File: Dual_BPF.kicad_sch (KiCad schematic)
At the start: 131 parts, among them J1 Conn_Coaxial, J2 Conn_Coaxial, J3 Conn_02x05_Odd_Even, K1 EE2-12NU, K10 EE2-12NU, K11 EE2-12NU, K12 EE2-12NU, K13 EE2-12NU, K14 EE2-12NU, K15 EE2-12NU, K2 EE2-12NU, K3 EE2-12NU, K4 EE2-12NU, K5 EE2-12NU, K6 EE2-12NU, K7 EE2-12NU, K8 EE2-12NU, K9 EE2-12NU, Q1 BSP250 /ZVP2106, U1 PGA-103, U2 RLP-30

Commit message: work in progress, 2 different pcb
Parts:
- removed D2: CD05_SOD323-T05, Diode_SMD:D_SOD-323, symbol Diode:SD05_SOD323
- removed K1, K10, K11, K12, K13, K14, K15, K2, K3, K4, K5, K6, K7, K8, K9: EE2-12NU, Relay_SMD:Relay_DPDT_Kemet_EE2_NU, symbol Relay:EE2-12NU
- removed U2: RLP-30, RF_Mini-Circuits:Mini-Circuits_GP1212_LandPatternPL-176, symbol RF_Filter:RLP-30
- added C100, C101, C102, C103, C104, C105, C106, C107, C108, C55, C56, C57, C58, C59, C60, C61, C62, C63, C64, C65, C66, C67, C68, C93, C94, C95, C96, C97, C98, C99: 10n, Capacitor_SMD:C_0805_2012Metric_Pad1.18x1.45mm_HandSolder, symbol Device:C_Small
- added C69, C71, C79: 100p, Capacitor_SMD:C_0805_2012Metric_Pad1.18x1.45mm_HandSolder, symbol Device:C_Small
- added C70, C73, C81, C92: 100n, Capacitor_SMD:C_0805_2012Metric_Pad1.18x1.45mm_HandSolder, symbol Device:C_Small
- added C72, C75, C88, C91: 470p, Capacitor_SMD:C_0805_2012Metric_Pad1.18x1.45mm_HandSolder, symbol Device:C_Small
- added C74, C87: 1n, Capacitor_SMD:C_0805_2012Metric_Pad1.18x1.45mm_HandSolder, symbol Device:C_Small
- added C76, C89: 270p, Capacitor_SMD:C_0805_2012Metric_Pad1.18x1.45mm_HandSolder, symbol Device:C_Small
- added C77, C78, C86, C90: 220p, Capacitor_SMD:C_0805_2012Metric_Pad1.18x1.45mm_HandSolder, symbol Device:C_Small
- added C80: 390p, Capacitor_SMD:C_0805_2012Metric_Pad1.18x1.45mm_HandSolder, symbol Device:C_Small
- added C82: 680p, Capacitor_SMD:C_0805_2012Metric_Pad1.18x1.45mm_HandSolder, symbol Device:C_Small
- added C83: 180p, Capacitor_SMD:C_0805_2012Metric_Pad1.18x1.45mm_HandSolder, symbol Device:C_Small
- added C84: 82p, Capacitor_SMD:C_0805_2012Metric_Pad1.18x1.45mm_HandSolder, symbol Device:C_Small
- added C85: 47p, Capacitor_SMD:C_0805_2012Metric_Pad1.18x1.45mm_HandSolder, symbol Device:C_Small
- added D2: SS36, Diode_SMD:D_SMB, symbol Device:D_Small
- added FB31, FB32, FB33, FB34, FB35, FB36, FB37, FB38, FB39, FB40, FB41, FB42, FB43, FB44, FB45, FB46, FB47, FB48, FB49, FB50, FB51, FB52, FB53, FB54, FB55, FB56, FB57, FB58, FB59, FB60: Ferrite, Inductor_SMD:L_0805_2012Metric, symbol Device:FerriteBead_Small
- added H1, H2, H3, H4, H5, H6, H7, H8: MountingHole_Pad, MountingHole:MountingHole_3.2mm_M3_ISO14580_Pad, symbol Mechanical:MountingHole_Pad
- added J4, J5: Conn_Coaxial, SMA_PINS:SMA_PINS, symbol Connector:Conn_Coaxial
- added J6: Conn_02x05_Odd_Even, Connector_IDC:IDC-Header_2x05_P2.54mm_Vertical, symbol Connector_Generic:Conn_02x05_Odd_Even
- added K1, K10, K11, K12, K13, K14, K15, K16, K17, K18, K19, K2, K20, K21, K22, K23, K24, K25, K26, K27, K28, K29, K3, K30, K4, K5, K6, K7, K8, K9: EC2-12NU, Relay_THT:Relay_DPDT_Kemet_EC2, symbol Relay:EC2-12NU
- added L18, L22, L24, L32: 330n, Inductor_SMD:L_1812_4532Metric_Pad1.30x3.40mm_HandSolder, symbol Device:L_Small
- added L19, L29, L34: 10u, Inductor_SMD:L_1812_4532Metric_Pad1.30x3.40mm_HandSolder, symbol Device:L_Small
- added L20, L26, L30: 1.8u, Inductor_SMD:L_1812_4532Metric_Pad1.30x3.40mm_HandSolder, symbol Device:L_Small
- added L21, L28, L31: 680n, Inductor_SMD:L_1812_4532Metric_Pad1.30x3.40mm_HandSolder, symbol Device:L_Small
- added L23, L33: 150n, Inductor_SMD:L_1812_4532Metric_Pad1.30x3.40mm_HandSolder, symbol Device:L_Small
- added L25: 2.7u, Inductor_SMD:L_1812_4532Metric_Pad1.30x3.40mm_HandSolder, symbol Device:L_Small
- added L27: 1u, Inductor_SMD:L_1812_4532Metric_Pad1.30x3.40mm_HandSolder, symbol Device:L_Small
- added Q2: BSP250 /ZVP2106, Package_TO_SOT_SMD:SOT-223-3_TabPin2, symbol Transistor_FET:FQP27P06
- added R10: 10k, Resistor_SMD:R_0805_2012Metric_Pad1.20x1.40mm_HandSolder, symbol Device:R_Small
- added R11, R12, R14, R18, R2, R3: 100R, Resistor_SMD:R_0805_2012Metric_Pad1.20x1.40mm_HandSolder, symbol Device:R_Small
- added R13, R15, R16: 62R, Resistor_SMD:R_0805_2012Metric_Pad1.20x1.40mm_HandSolder, symbol Device:R_Small
- added R17: 30R, Resistor_SMD:R_0805_2012Metric_Pad1.20x1.40mm_HandSolder, symbol Device:R_Small
- added U2: PGA-103, Package_TO_SOT_SMD:SOT-89-3, symbol RF_Amplifier:PGA-103
- C15, C17: value C_Small -> 100p
- C16, C19: value C_Small -> 100n
- C18, C21: value C_Small -> 470p
- C20: value C_Small -> 1n
- C22: value C_Small -> 270p
- C23, C24: value C_Small -> 220p
- C25: renamed from C26; value C_Small -> 100p
- C26: renamed from C27; value C_Small -> 390p
- C27: renamed from C28; value C_Small -> 100n
- C28: renamed from C29; value C_Small -> 680p
- C29: renamed from C30; value C_Small -> 180p
- C30: renamed from C31; value C_Small -> 82p
- C31: renamed from C32; value C_Small -> 47p
- C32: renamed from C33; value C_Small -> 220p
- C33: renamed from C35; value C_Small -> 1n
- C34: renamed from C36; value C_Small -> 470p
- C35: renamed from C37; value C_Small -> 270p
- C36: renamed from C38; value C_Small -> 220p
- C37: renamed from C39; value C_Small -> 470p
- C38: renamed from C25; value C_Small -> 100n
- D1: value D_Small -> SS36; footprint (none) -> Diode_SMD:D_SMB
- FB1, FB10, FB11, FB12, FB13, FB14, FB15, FB16, FB17, FB18, FB19, FB2, FB20, FB21, FB22, FB23, FB24, FB25, FB26, FB27, FB28, FB29, FB3, FB30, FB4, FB5, FB6, FB7, FB8, FB9: footprint (none) -> Inductor_SMD:L_0805_2012Metric
- J1, J2: footprint (none) -> SMA_PINS:SMA_PINS
- J3: footprint (none) -> Connector_IDC:IDC-Header_2x05_P2.54mm_Vertical
- L1, L15, L5, L7: value L_Small -> 330n; footprint (none) -> Amidon_T50:T50_V_THT_1812_merge
- L10: value L_Small -> 1u; footprint (none) -> Amidon_T50:T50_V_THT_1812_merge
- L11, L14, L4: value L_Small -> 680n; footprint (none) -> Amidon_T50:T50_V_THT_1812_merge
- L12, L17, L2: value L_Small -> 10u; footprint (none) -> Amidon_T50:T50_V_THT_1812_merge
- L13, L3, L9: value L_Small -> 1.8u; footprint (none) -> Amidon_T50:T50_V_THT_1812_merge
- L16, L6: value L_Small -> 150n; footprint (none) -> Amidon_T50:T50_V_THT_1812_merge
- L8: value L_Small -> 2.7u; footprint (none) -> Amidon_T50:T50_V_THT_1812_merge
- Q1: footprint Package_TO_SOT_THT:TO-220-3_Vertical -> Package_TO_SOT_SMD:SOT-223-3_TabPin2
- R1: renamed from R4; value R_Small -> 10k; footprint (none) -> Resistor_SMD:R_0805_2012Metric_Pad1.20x1.40mm_HandSolder
- R4: renamed from R2; value R_Small -> 62R; footprint (none) -> Resistor_SMD:R_0805_2012Metric_Pad1.20x1.40mm_HandSolder
- R5: renamed from R1; value R_Small -> 100R; footprint (none) -> Resistor_SMD:R_0805_2012Metric_Pad1.20x1.40mm_HandSolder
- R6: renamed from R3; value R_Small -> 62R; footprint (none) -> Resistor_SMD:R_0805_2012Metric_Pad1.20x1.40mm_HandSolder
- R7: renamed from R5; value R_Small -> 62R; footprint (none) -> Resistor_SMD:R_0805_2012Metric_Pad1.20x1.40mm_HandSolder
- R8: renamed from R6; value R_Small -> 30R; footprint (none) -> Resistor_SMD:R_0805_2012Metric_Pad1.20x1.40mm_HandSolder
- R9: renamed from R7; value R_Small -> 100R; footprint (none) -> Resistor_SMD:R_0805_2012Metric_Pad1.20x1.40mm_HandSolder
- renumbered C40 to C39, C41 to C40, C42 to C41, C43 to C42, C44 to C43, C45 to C44, C46 to C45, C47 to C46, C48 to C47, C49 to C48, C50 to C49, C51 to C50, C52 to C51, C34 to C52
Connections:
- net +12V: now also C81.1, FB32.1, FB34.1, FB36.1, FB38.1, FB40.1, FB42.1, FB44.1, FB46.1, FB48.1, FB50.1, FB52.1, FB54.1, FB56.1, FB58.1, FB60.1, J6.9 (Pin_9), Q2.3 (S), R10.1
- net 1.5HPF: now also FB33.1, FB47.1, J6.5 (Pin_5)
- net 13HPF: now also FB39.1, FB53.1, J6.2 (Pin_2)
- net 20HPF: now also FB41.1, FB55.1, J6.1 (Pin_1)
- net 6.5HPF: now also FB35.1, FB49.1, J6.4 (Pin_4)
- net 6mLNA: now also C70.1, D2.1 (K), FB31.1, FB59.1, J6.6 (Pin_6)
- net 9.5HPF: now also FB37.1, FB51.1, J6.3 (Pin_3)
- net GND: now also C100.2, C101.2, C102.2, C103.2, C104.2, C105.2, C106.1, C107.2, C108.2, C55.2, C56.2, C57.2, C58.2, C59.2, C60.2, C61.2, C62.2, C63.2, C64.2, C65.2, C66.2, C67.2, C68.2, C70.2, C72.2, C73.1, C74.2, C75.2, C76.2, C77.2, C80.1, C81.2, C87.1, C88.1, C89.1, C90.1, C91.2, C93.2, C94.2, C95.2, C96.2, C97.2, C98.2, C99.2, H1.1, H2.1, H3.1, H4.1, H5.1, H6.1, H7.1, H8.1, J4.2 (Ext), J5.2 (Ext), J6.10 (Pin_10), K1.10, K1.3, K10.10, K10.3, K11.10, K11.3, K12.10, K12.3, K13.10, K13.3, K14.10, K14.3, K15.10, K15.3, K16.10, K16.3, K17.10, K17.3, K18.10, K18.3, K19.10, K19.3, K2.10, K2.3, K20.10, K20.3, K21.10, K21.3, K22.10, K22.3, K24.10, K24.3, K25.10, K25.3, K26.10, K26.3, K27.10, K27.3, K28.10, K28.3, K29.10, K29.3, K3.10, K3.3, K30.10, K30.3, K4.10, K4.3, K5.10, K5.3, K6.10, K6.3, K7.10, K7.3, K9.10, K9.3, L18.2, L20.1, L21.1, L22.1, L23.1, L24.2, L29.2, L30.2, L31.2, L32.2, L33.2, R11.2, R12.1, R14.2, R18.1, R2.2, R3.1, U2.2 (GND)
- net HPF_ByPass: now also FB43.1, FB57.1, J6.8 (Pin_8)
- net RX2_GND: now also FB45.1, J6.7 (Pin_7)
- net at C12.1, FB10.2: now also K5.1
- net at C6.1, FB9.2: now also K5.12
- net at C22.1, L10.1, L5.2: now also K5.4, K5.9
- net at C29.1, C34.2, L14.1: now also K11.4, K11.9
- net at C49.1, FB23.2: now also K12.12
- net at C52.2, FB16.2: now also K8.1
- net at C39.1, FB15.2: now also K8.12
- net at J2.1 (In): now also K8.10, K8.3, K8.5, K8.8, R2.1, R3.2
- net at C25.1, U1.1: no longer C38.1, R7.2
- net at U1.3: now also C38.2, R7.2; no longer R8.2
- net at C43.1, FB24.2: now also K12.1
- net at C41.1, FB20.2: now also K10.1
- net at C30.1, C35.2, L15.1: now also K12.4, K12.9
- net at C53.1, FB30.2: now also K15.1
- net at C44.1, FB26.2: now also K13.1
- net at C46.1, FB17.2: now also K9.12
- net at C28.1, C33.2, L13.1: now also K10.4, K10.9
- net at C21.1, L4.2, L9.1: now also K4.4, K4.9
- net at C15.2: now also K1.4, K1.9
- net at C54.1, FB29.2: now also K15.12
- net at J1.1 (In): now also K10.5, K10.8, K11.5, K11.8, K12.5, K12.8, K13.5, K13.8, K14.5, K14.8, K15.5, K15.8, K9.5, K9.8
- net at C9.1, FB4.2: now also K2.1
- net at C47.1, FB19.2: now also K10.12
- net at C31.1, C36.2, L16.1: now also K13.4, K13.9
- net at C45.1, FB28.2: now also K14.1
- net at R5.1: now also C38.1, R8.2; no longer C38.2
- net at C1.1, FB1.2: now also K1.12
- net at R8.1, R9.2: now also K15.4, K15.9
- net at C13.1, FB12.2: now also K6.1
- net at C8.1, FB13.2: now also K7.12
- net at C10.1, FB6.2: now also K3.1
- net at L2.2: now also K2.4, K2.9
- net at C2.1, FB2.2: now also K1.1
- net at L17.1: now also K9.4, K9.9
- net at C20.1, L3.2, L8.1: now also K3.4, K3.9
- net at C50.1, FB25.2: now also K13.12
- net at C7.1, FB11.2: now also K6.12
- net at C11.1, FB8.2: now also K4.1
- net at C4.1, FB5.2: now also K3.12
- net at C42.1, FB22.2: now also K11.1
- net at C14.1, FB14.2: now also K7.1
- net at C40.1, FB18.2: now also K9.1
- net at C51.1, FB27.2: now also K14.12
- net at C23.1, L11.1, L6.2: now also K6.4, K6.9
- net at C5.1, FB7.2: now also K4.12
- net at C48.1, FB21.2: now also K11.12
- net at C3.1, FB3.2: now also K2.12
- new net: C68.1, FB44.2, K22.1
- new net: J5.1 (In), K23.10, K23.3
- new net: C108.1, FB59.2, K30.12
- new net: C65.1, FB38.2, K19.1
- new net: C59.1, FB37.2, K19.12
- new net: C75.1, K19.4, K19.9, L21.2, L26.1
- new net: K16.5, K16.8, K17.5, K17.8, K18.5, K18.8, K19.5, K19.8, K20.5, K20.8, K21.5, K21.8, K22.5, K22.8, K23.4, K23.9
- new net: K1.5, K1.8, K2.5, K2.8, K3.5, K3.8, K4.5, K4.8, K5.5, K5.8, K6.5, K6.8, K7.5, K7.8, K8.4, K8.9
- new net: C74.1, K18.4, K18.9, L20.2, L25.1
- new net: C82.2, L25.2
- new net: C84.1, C89.2, K27.4, K27.9, L32.1
- new net: C57.1, FB33.2, K17.12
- new net: C58.1, FB35.2, K18.12
- new net: C86.2, C91.1, L34.2
- new net: C77.1, K21.4, K21.9, L23.2, L28.1
- new net: C69.1, C71.2, L18.1
- new net: C101.1, FB49.2, K25.12
- new net: C85.2, L28.2
- new net: C83.2, L26.2
- new net: K14.4, K14.9, K7.4, K7.9
- new net: K23.5, K23.8, R11.1, R12.2
- new net: C85.1, C90.2, K28.4, K28.9, L33.1
- new net: C61.1, FB41.2, K21.12
- new net: C63.1, FB34.2, K17.1
- new net: K17.4, K17.9, L19.2
- new net: C92.1, R14.1, R17.2
- new net: C83.1, C88.2, K26.4, K26.9, L31.1
- new net: C67.1, FB42.2, K21.1
- new net: C55.1, FB31.2, K16.12
- new net: K24.4, K24.9, L34.1
- new net: C66.1, FB40.2, K20.1
- new net: C60.1, FB39.2, K20.12
- new net: C76.1, K20.4, K20.9, L22.2, L27.1
- new net: C69.2, K16.4, K16.9
- new net: C95.1, FB50.2, K25.1
- new net: C82.1, C87.2, K25.4, K25.9, L30.1
- new net: J4.1 (In), K24.5, K24.8, K25.5, K25.8, K26.5, K26.8, K27.5, K27.8, K28.5, K28.8, K29.5, K29.8, K30.5, K30.8
- new net: C78.2, C80.2, C86.1, L29.1
- new net: R15.2, R16.1
- new net: C92.2, R16.2, U2.3
- new net: C72.1, C78.1, L19.1
- new net: C84.2, L27.2
- new net: C93.1, FB45.2, K23.12
- new net: C103.1, FB53.2, K27.12
- new net: K30.4, K30.9, R17.1, R18.2
- new net: C71.1, C79.2, L24.1
- new net: C96.1, FB52.2, K26.1
- new net: C102.1, FB51.2, K26.12
- new net: C97.1, FB54.2, K27.1
- new net: C106.2, FB46.2, K23.1
- new net: C64.1, FB36.2, K18.1
- new net: C107.1, FB60.2, K30.1
- new net: C62.1, FB43.2, K22.12
- new net: C73.2, Q2.2 (D), R13.1
- new net: R13.2, R15.1
- new net: D2.2 (A), Q2.1 (G), R10.2
- new net: C94.1, FB48.2, K24.1
- new net: C105.1, FB57.2, K29.12
- new net: C104.1, FB55.2, K28.12
- new net: C79.1, U2.1
- new net: C98.1, FB56.2, K28.1
- new net: C100.1, FB47.2, K24.12
- new net: C99.1, FB58.2, K29.1
- new net: K22.4, K22.9, K29.4, K29.9
- new net: C56.1, FB32.2, K16.1
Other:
- note added: "All relays EE2-12NU (gull wing) or EC2-12NU (through)"
- note removed: "SOD-323-2"
- moved on the sheet: C38, C39, C52, FB15, FB16, J2, R4, R5, R6, R7, R8, R9

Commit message: SMD version RTM 1.0, toroid version deleted
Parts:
- removed C1, C10, C11, C12, C13, C14, C2, C3, C39, C4, C40, C41, C42, C43, C44, C45, C46, C47, C48, C49, C5, C50, C51, C52, C53, C54, C6, C7, C8, C9: 10n, Capacitor_SMD:C_0805_2012Metric_Pad1.18x1.45mm_HandSolder, symbol Device:C_Small
- removed C15, C17, C25: 100p, Capacitor_SMD:C_0805_2012Metric_Pad1.18x1.45mm_HandSolder, symbol Device:C_Small
- removed C16, C19, C27, C38: 100n, Capacitor_SMD:C_0805_2012Metric_Pad1.18x1.45mm_HandSolder, symbol Device:C_Small
- removed C18, C21, C34, C37: 470p, Capacitor_SMD:C_0805_2012Metric_Pad1.18x1.45mm_HandSolder, symbol Device:C_Small
- removed C20, C33: 1n, Capacitor_SMD:C_0805_2012Metric_Pad1.18x1.45mm_HandSolder, symbol Device:C_Small
- removed C22, C35: 270p, Capacitor_SMD:C_0805_2012Metric_Pad1.18x1.45mm_HandSolder, symbol Device:C_Small
- removed C23, C24, C32, C36: 220p, Capacitor_SMD:C_0805_2012Metric_Pad1.18x1.45mm_HandSolder, symbol Device:C_Small
- removed C26: 390p, Capacitor_SMD:C_0805_2012Metric_Pad1.18x1.45mm_HandSolder, symbol Device:C_Small
- removed C28: 680p, Capacitor_SMD:C_0805_2012Metric_Pad1.18x1.45mm_HandSolder, symbol Device:C_Small
- removed C29: 180p, Capacitor_SMD:C_0805_2012Metric_Pad1.18x1.45mm_HandSolder, symbol Device:C_Small
- removed C30: 82p, Capacitor_SMD:C_0805_2012Metric_Pad1.18x1.45mm_HandSolder, symbol Device:C_Small
- removed C31: 47p, Capacitor_SMD:C_0805_2012Metric_Pad1.18x1.45mm_HandSolder, symbol Device:C_Small
- removed D1: SS36, Diode_SMD:D_SMB, symbol Device:D_Small
- removed FB1, FB10, FB11, FB12, FB13, FB14, FB15, FB16, FB17, FB18, FB19, FB2, FB20, FB21, FB22, FB23, FB24, FB25, FB26, FB27, FB28, FB29, FB3, FB30, FB4, FB5, FB6, FB7, FB8, FB9: Ferrite, Inductor_SMD:L_0805_2012Metric, symbol Device:FerriteBead_Small
- removed H1, H2, H3, H4: MountingHole_Pad, MountingHole:MountingHole_3.2mm_M3_ISO14580_Pad, symbol Mechanical:MountingHole_Pad
- removed J1, J2: Conn_Coaxial, SMA_PINS:SMA_PINS, symbol Connector:Conn_Coaxial
- removed J3: Conn_02x05_Odd_Even, Connector_IDC:IDC-Header_2x05_P2.54mm_Vertical, symbol Connector_Generic:Conn_02x05_Odd_Even
- removed K1, K10, K11, K12, K13, K14, K15, K2, K3, K4, K5, K6, K7, K8, K9: EC2-12NU, Relay_THT:Relay_DPDT_Kemet_EC2, symbol Relay:EC2-12NU
- removed L1, L15, L5, L7: 330n, Amidon_T50:T50_V_THT_1812_merge, symbol Device:L_Small
- removed L10: 1u, Amidon_T50:T50_V_THT_1812_merge, symbol Device:L_Small
- removed L11, L14, L4: 680n, Amidon_T50:T50_V_THT_1812_merge, symbol Device:L_Small
- removed L12, L17, L2: 10u, Amidon_T50:T50_V_THT_1812_merge, symbol Device:L_Small
- removed L13, L3, L9: 1.8u, Amidon_T50:T50_V_THT_1812_merge, symbol Device:L_Small
- removed L16, L6: 150n, Amidon_T50:T50_V_THT_1812_merge, symbol Device:L_Small
- removed L8: 2.7u, Amidon_T50:T50_V_THT_1812_merge, symbol Device:L_Small
- removed Q1: BSP250 /ZVP2106, Package_TO_SOT_SMD:SOT-223-3_TabPin2, symbol Transistor_FET:FQP27P06
- removed R1: 10k, Resistor_SMD:R_0805_2012Metric_Pad1.20x1.40mm_HandSolder, symbol Device:R_Small
- removed R2, R3, R5, R9: 100R, Resistor_SMD:R_0805_2012Metric_Pad1.20x1.40mm_HandSolder, symbol Device:R_Small
- removed R4, R6, R7: 62R, Resistor_SMD:R_0805_2012Metric_Pad1.20x1.40mm_HandSolder, symbol Device:R_Small
- removed R8: 30R, Resistor_SMD:R_0805_2012Metric_Pad1.20x1.40mm_HandSolder, symbol Device:R_Small
- removed U1: PGA-103, Package_TO_SOT_SMD:SOT-89-3, symbol RF_Amplifier:PGA-103
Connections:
- net 1.5HPF renamed 1.5HPF_2
- net 13HPF renamed 13HPF_2
- net 20HPF renamed 20HPF_2
- net 6.5HPF renamed 6.5HPF_2
- net 6mLNA renamed 6mLNA_2
- net 9.5HPF renamed 9.5HPF_2
- net HPF_ByPass renamed HPF_ByPass_2
- net RX2_GND renamed RX2_GND_2
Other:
- moved on the sheet: C100, C101, C102, C103, C104, C105, C106, C107, C108, C55, C56, C57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

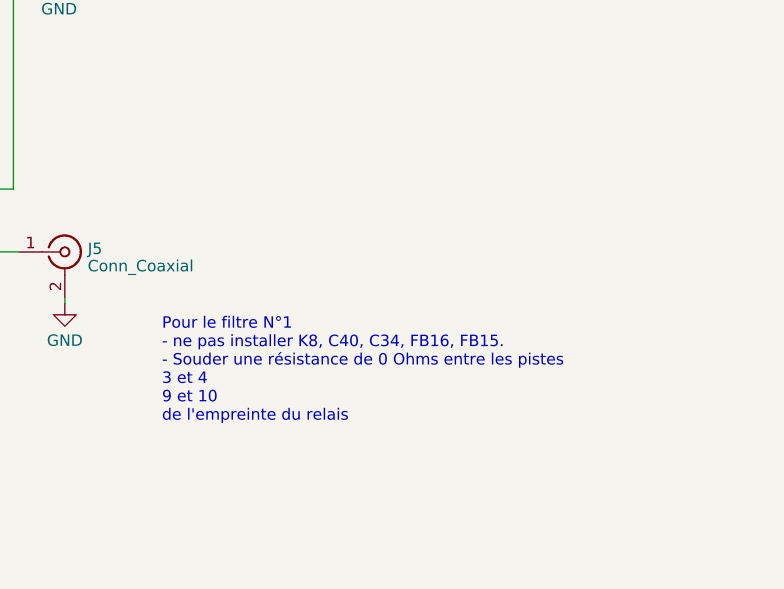
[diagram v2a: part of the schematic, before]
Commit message: small mods on schematic comments
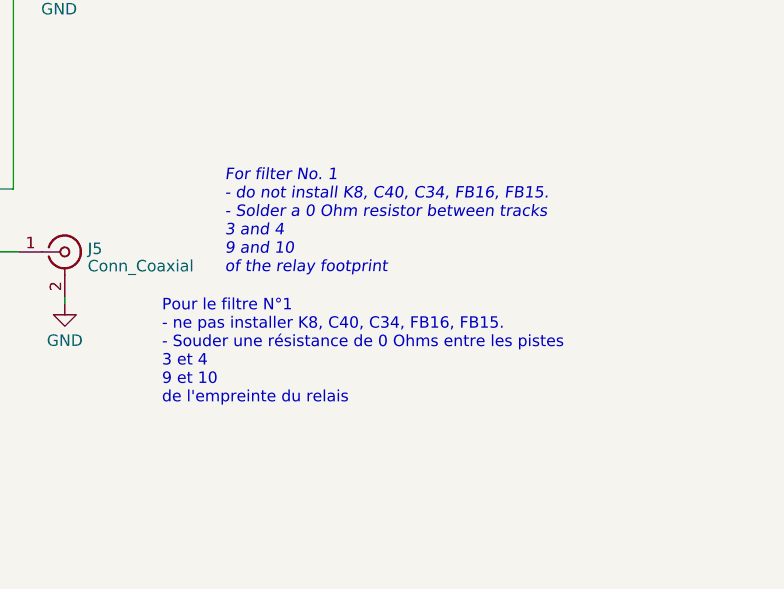
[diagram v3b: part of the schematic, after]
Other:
- note added: "For filter No. 1 - do not install K8, C40, C34, FB16, FB15. - Solder a 0 Ohm resistor between tracks 3 and 4 9 and 10 of the relay footprint"
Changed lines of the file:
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@@
     (stroke (width 0) (type default))
   )
-  (text "Pour le filtre N°1\n- ne pas installer K8, C40, C34, FB16, FB15. \n- Souder une résistance de 0 Ohms entre les pistes \n3 et 4\n9 et 10 \nde l'empreinte du relais"
+  (text "Pour le filtre N°1\n- ne pas installer K8, C40, C34, FB16, FB15. \n- Souder une résistance de 0 Ohms entre les pistes \n3 et 4\n9 et 10 \nde l'empreinte du relais\n\n"
     (at 145.415 247.65 0)
     (effects (font (size 1.27 1.27)) (justify left bottom))
@@
     (effects (font (size 1.27 1.27)) (justify left bottom))
   )
+  (text "For filter No. 1\n- do not install K8, C40, C34, FB16, FB15. \n- Solder a 0 Ohm resistor between tracks \n3 and 4\n9 and 10 \nof the relay footprint"
+    (at 152.4 231.14 0)
+    (effects (font (size 1.27 1.27) italic) (justify left bottom))
+  )
   (global_label "13HPF_2" (shape input) (at 123.825 110.49 270) (fields_autoplaced)

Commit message: minor changes and new iBom
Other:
- note added: "For filter No. 1 - do not install K23, C40, C34, FB16, FB15. - Solder a 0 Ohm resistor between tracks 3 and 4 9 and 10 of the K23 relay footprint"
- note added: "Pour le filtre N°1 - ne pas installer K23, C40, C34, FB16, FB15. - Souder une résistance de 0 Ohms entre les pistes 3 et 4 9 et 10 de l'empreinte du relais K23"
- note removed: "For filter No. 1 - do not install K8, C40, C34, FB16, FB15. - Solder a 0 Ohm resistor between tracks 3 and 4 9 and 10 of the relay footprint"
- note removed: "Pour le filtre N°1 - ne pas installer K8, C40, C34, FB16, FB15. - Souder une résistance de 0 Ohms entre les pistes 3 et 4 9 et 10 de l'empreinte du relais"
